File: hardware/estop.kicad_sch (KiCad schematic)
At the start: 2 parts

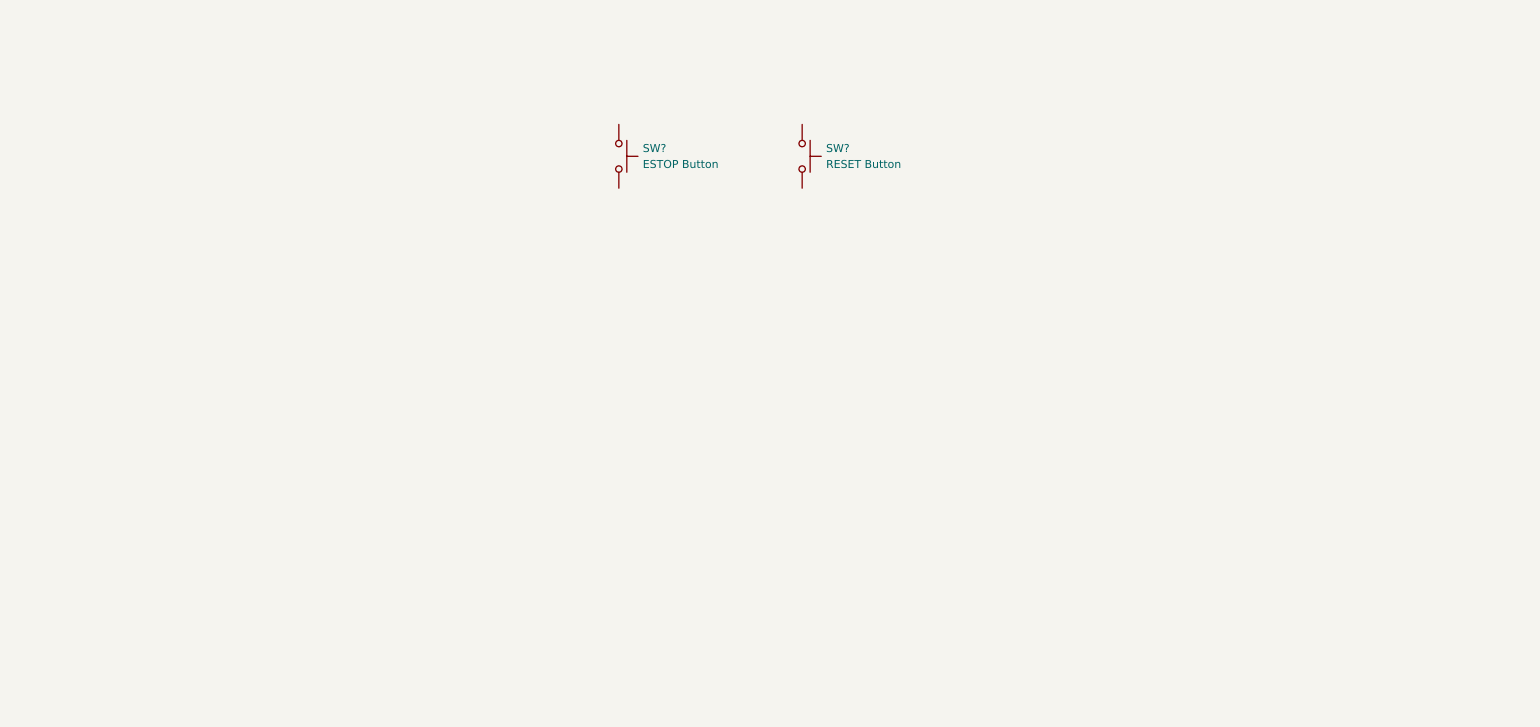
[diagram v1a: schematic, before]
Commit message: Begin ESTOP sheet
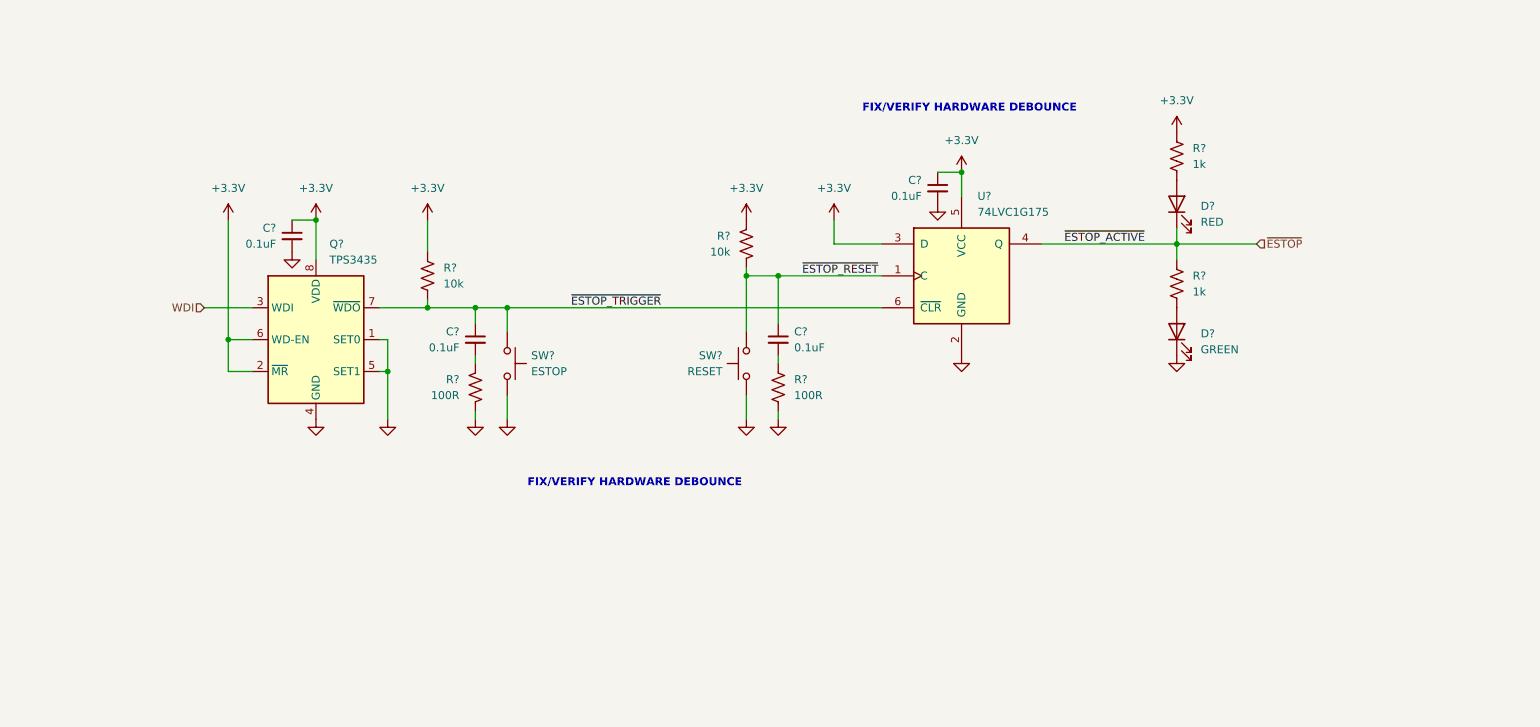
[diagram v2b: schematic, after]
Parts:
- added C? (x4): 0.1uF, Capacitor_SMD:C_0603_1608Metric_Pad1.08x0.95mm_HandSolder, symbol Device:C_Small
- added D?: GREEN, Diode_SMD:D_0805_2012Metric, symbol Device:LED
- added D?: RED, Diode_SMD:D_0805_2012Metric, symbol Device:LED
- added Q?: TPS3435, Package_TO_SOT_SMD:SOT-23-8, symbol stepping-stone:TPS3435CAGBJDDFRQ1
- added R? (x2): 10k, Resistor_SMD:R_0603_1608Metric, symbol Device:R_US
- added R? (x2): 1k, Resistor_SMD:R_0603_1608Metric, symbol Device:R_US
- added R? (x2): 100R, Resistor_SMD:R_0603_1608Metric, symbol Device:R_US
- added U?: 74LVC1G175, Package_TO_SOT_SMD:SOT-23-6, symbol 74xGxx:74LVC1G175
- SW?: value RESET Button -> RESET
- SW?: value ESTOP Button -> ESTOP
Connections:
- net ~{ESTOP_RESET}: now reaches SW?.1
- net ~{ESTOP_RESET}: now also C?.1, R?.2, U?.1 (C)
- net GND: now reaches SW?.2
- net GND: now also SW?.2, C?.2, C?.2, D?.1 (K), Q?.1 (SET0), Q?.4 (GND), Q?.5 (SET1), R?.1, R?.1, U?.2 (GND)
- net ~{ESTOP_TRIGGER}: now reaches SW?.1
- net ~{ESTOP_TRIGGER}: now also C?.1, Q?.7 (~{WDO}), R?.2, U?.6 (~{CLR})
- new net: D?.2 (A), R?.2 (x2)
- new net: C?.2, R?.2 (x2)
- new net +3.3V: C?.1, C?.1, Q?.2 (~{MR}), Q?.6 (WD-EN), Q?.8 (VDD), R?.1, R?.1, R?.1, U?.3 (D), U?.5 (VCC)
- new net WDI: Q?.3 (WDI)
- new net ~{ESTOP}: D?.1 (K), R?.1, U?.4 (Q)
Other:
- note added: "FIX/VERIFY HARDWARE DEBOUNCE"
- company: (none) -> Jacob Wigent
- title: (none) -> ESTOP System
- moved on the sheet: SW?

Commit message: Random changes & LED additions
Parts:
- U?: Part Number (none) -> SN74LVC1G175DBVR; Vendor URL (none) -> https://www.digikey.com/en/products/detail/texas-instrument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
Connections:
- net ~{ESTOP_TRIGGER} renamed ~{EXT_TRIG}
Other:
- note added: "ESTOP Button"
- note added: "ESTOP Triggers"
- note added: "External"
- note added: "External trigger should be driven by OPEN-DRAIN GPIO for safety."
- note added: "FIX/VERIFY HARDWARE DEBOUNCE FOR BOTH BUTTONS 74LVC MAY NEED SCHMITT TRIG INPUTS"
- note added: "Heartbeat Watchdog"
- note removed: "FIX/VERIFY HARDWARE DEBOUNCE"
- moved on the sheet: C?, D?, Q?, R?, SW?, U?

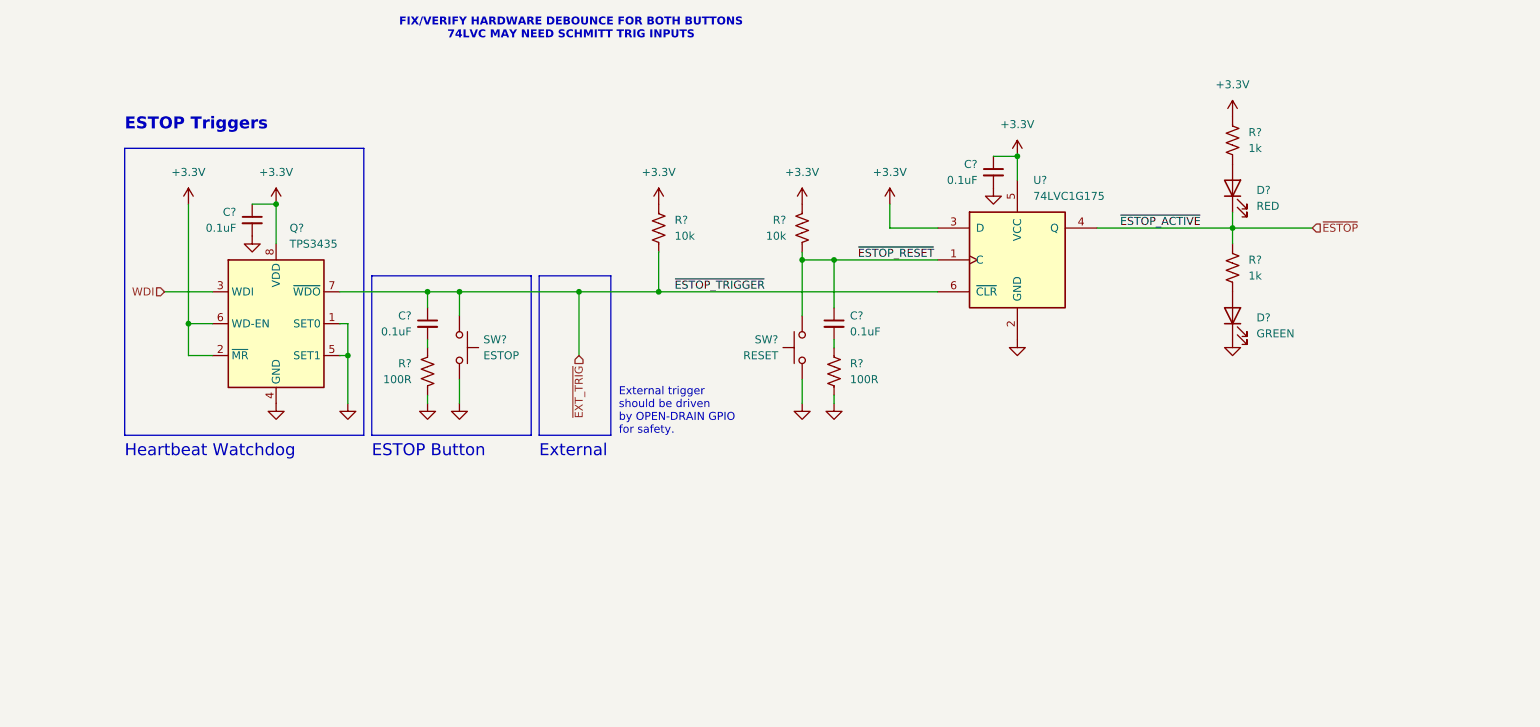
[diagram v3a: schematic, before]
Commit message: ESTOP control refinement
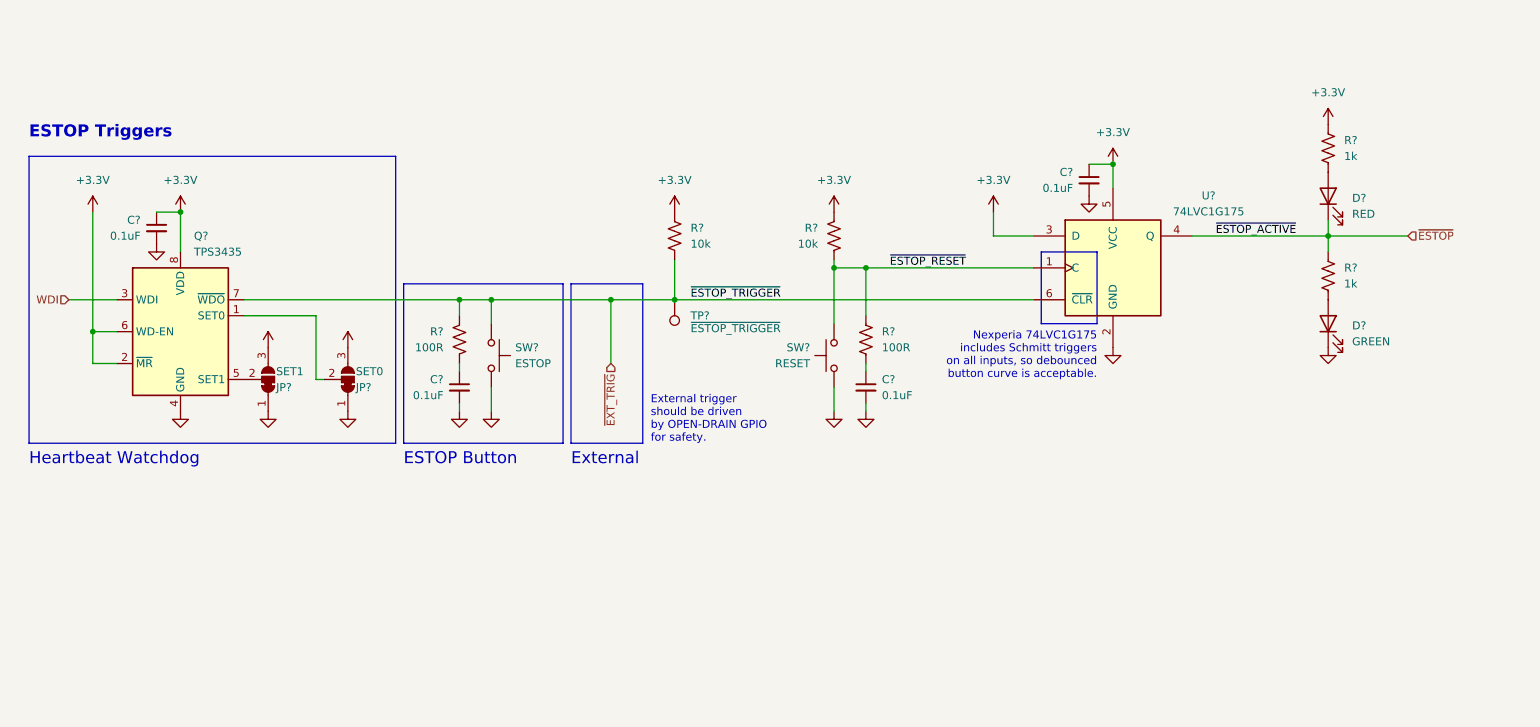
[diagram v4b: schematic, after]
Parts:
- removed C?: 0.1uF, Capacitor_SMD:C_0603_1608Metric_Pad1.08x0.95mm_HandSolder, symbol Device:C_Small
- removed R?: 100R, Resistor_SMD:R_0603_1608Metric, symbol Device:R_US
- removed U?: 74LVC1G175, Package_TO_SOT_SMD:SOT-23-6, symbol 74xGxx:74LVC1G175
- added C?: 0.1uF, Capacitor_SMD:C_0603_1608Metric_Pad1.08x0.95mm_HandSolder, symbol Device:C_Small
- added JP?: SET0, Jumper:SolderJumper-3_P1.3mm_Bridged12_RoundedPad1.0x1.5mm, symbol Jumper:SolderJumper_3_Bridged12
- added JP?: SET1, Jumper:SolderJumper-3_P1.3mm_Bridged12_RoundedPad1.0x1.5mm, symbol Jumper:SolderJumper_3_Bridged12
- added R?: 100R, Resistor_SMD:R_0603_1608Metric, symbol Device:R_US
- added TP?: ~{ESTOP_TRIGGER}, TestPoint:TestPoint_Pad_D1.0mm, symbol Connector:TestPoint
- added U?: 74LVC1G175, Package_TO_SOT_SMD:SOT-363_SC-70-6, symbol 74xGxx:74LVC1G175
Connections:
- net +3.3V: now also JP?.3 (B), JP?.3 (B), U?.3 (D), U?.5 (VCC)
- net GND: now also C?.2, C?.2, JP?.1 (A), JP?.1 (A), U?.2 (GND); no longer Q?.1 (SET0), Q?.5 (SET1), R?.1
- net ~{ESTOP_RESET}: now also R?.2, U?.1 (C)
- net ~{ESTOP}: now also U?.4 (Q)
- net ~{EXT_TRIG}: now also R?.2, TP?.1, U?.6 (~{CLR}); no longer C?.1
- new net: JP?.2 (C), Q?.1 (SET0)
- new net: JP?.2 (C), Q?.5 (SET1)
- new net: C?.1, R?.1 (x2)
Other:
- note added: "Nexperia 74LVC1G175 includes Schmitt triggers on all inputs, so debounced button curve is acceptable."
- note removed: "FIX/VERIFY HARDWARE DEBOUNCE FOR BOTH BUTTONS 74LVC MAY NEED SCHMITT TRIG INPUTS"
- moved on the sheet: C?, D?, Q?, R?, SW?

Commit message: SD Card Pull Ups and ESD
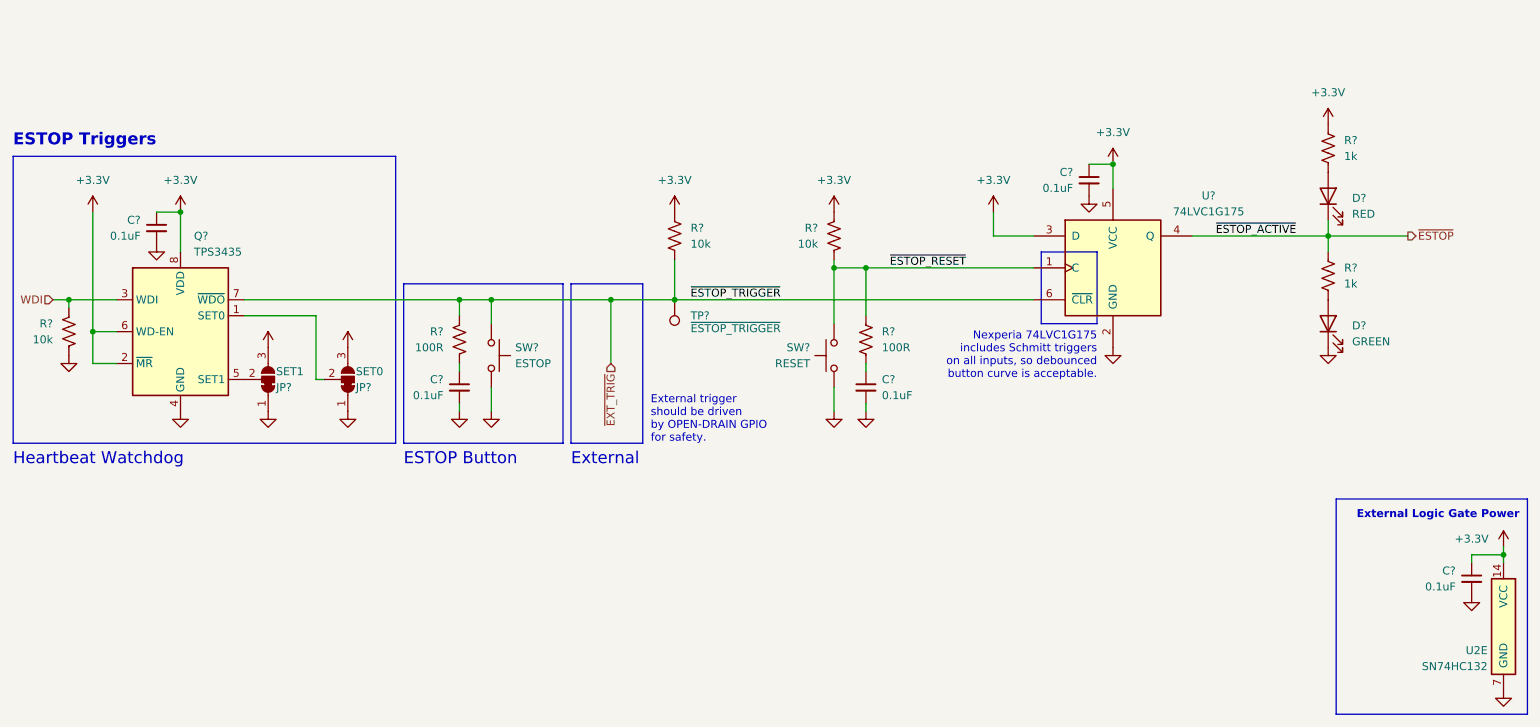
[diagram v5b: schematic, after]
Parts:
- added C?: 0.1uF, Capacitor_SMD:C_0603_1608Metric_Pad1.08x0.95mm_HandSolder, symbol Device:C_Small
- added R?: 10k, Resistor_SMD:R_0603_1608Metric, symbol Device:R_US
- added U2: SN74HC132, Package_SO:SOIC-14_3.9x8.7mm_P1.27mm, symbol stepping-stone:SN74LVC08
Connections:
- net +3.3V: now also C?.1, U2.14 (VCC)
- net GND: now also C?.2, R?.2, U2.7 (GND)
- net WDI: now also R?.1
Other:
- note added: "External Logic Gate Power"

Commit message: Add QSPI Flash
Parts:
- gave numbers to parts that had none: 21
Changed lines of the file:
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@@
 		(in_pos_files yes)
 		(dnp no)
-		(property "Reference" "R?"
+		(property "Reference" "R22"
 			(at 31.75 109.2199 0)
 			(show_name no)
@@
 			(project "stepping-stone"
 				(path "/793a882e-3f7b-468b-a863-41a1f527e1bf/ca68e3e0-6620-4c6d-b672-8e352c5602f5"
-					(reference "R?")
+					(reference "R22")
 					(unit 1)
 				)
@@
 		(in_pos_files yes)
 		(dnp no)
-		(property "Reference" "R?"
+		(property "Reference" "R19"
 			(at 133.35 93.9799 0)
 			(show_name no)
@@
 			(project "stepping-stone"
 				(path "/793a882e-3f7b-468b-a863-41a1f527e1bf/ca68e3e0-6620-4c6d-b672-8e352c5602f5"
-					(reference "R?")
+					(reference "R19")
 					(unit 1)
 				)
@@
 		(in_pos_files yes)
 		(dnp no)
-		(property "Reference" "C?"
+		(property "Reference" "C13"
 			(at 45.72 92.71 0)
 			(show_name no)
@@
 			(project "stepping-stone"
 				(path "/793a882e-3f7b-468b-a863-41a1f527e1bf/ca68e3e0-6620-4c6d-b672-8e352c5602f5"
-					(reference "C?")
+					(reference "C13")
 					(unit 1)
 				)
@@
 		(in_pos_files yes)
 		(dnp no)
-		(property "Reference" "R?"
+		(property "Reference" "R20"
 			(at 153.67 93.9799 0)
 			(show_name no)
@@
 			(project "stepping-stone"
 				(path "/793a882e-3f7b-468b-a863-41a1f527e1bf/ca68e3e0-6620-4c6d-b672-8e352c5602f5"
-					(reference "R?")
+					(reference "R20")
 					(unit 1)
 				)
@@
 		(dnp no)
 		(fields_autoplaced yes)
-		(property "Reference" "Q?"
+		(property "Reference" "Q3"
 			(at 54.2133 95.25 0)
 			(show_name no)
@@
 			(project "stepping-stone"
 				(path "/793a882e-3f7b-468b-a863-41a1f527e1bf/ca68e3e0-6620-4c6d-b672-8e352c5602f5"
-					(reference "Q?")
+					(reference "Q3")
 					(unit 1)
 				)
@@
 		(in_pos_files yes)
 		(dnp no)
-		(property "Reference" "SW?"
+		(property "Reference" "SW8"
 			(at 152.4 113.03 90)
 			(show_name no)
@@
 			(project "stepping-stone"
 				(path "/793a882e-3f7b-468b-a863-41a1f527e1bf/ca68e3e0-6620-4c6d-b672-8e352c5602f5"
-					(reference "SW?")
+					(reference "SW8")
 					(unit 1)
 				)
@@
 		(in_pos_files yes)
 		(dnp no)
-		(property "Reference" "C?"
+		(property "Reference" "C15"
 			(at 163.83 118.1162 0)
 			(show_name no)
@@
 			(project "stepping-stone"
 				(path "/793a882e-3f7b-468b-a863-41a1f527e1bf/ca68e3e0-6620-4c6d-b672-8e352c5602f5"
-					(reference "C?")
+					(reference "C15")
 					(unit 1)
 				)
@@
 		(in_pos_files yes)
 		(dnp no)
-		(property "Reference" "TP?"
+		(property "Reference" "TP1"
 			(at 133.35 107.95 0)
 			(show_name no)
@@
 			(project "stepping-stone"
 				(path "/793a882e-3f7b-468b-a863-41a1f527e1bf/ca68e3e0-6620-4c6d-b672-8e352c5602f5"
-					(reference "TP?")
+					(reference "TP1")
 					(unit 1)
 				)
@@
 		(dnp no)
 		(fields_autoplaced yes)
-		(property "Reference" "R?"
+		(property "Reference" "R21"
 			(at 237.49 100.3299 0)
 			(show_name no)
@@
 			(project "stepping-stone"
 				(path "/793a882e-3f7b-468b-a863-41a1f527e1bf/ca68e3e0-6620-4c6d-b672-8e352c5602f5"
-					(reference "R?")
+					(reference "R21")
 					(unit 1)
 				)
@@
 		(dnp no)
 		(fields_autoplaced yes)
-		(property "Reference" "D?"
+		(property "Reference" "D11"
 			(at 238.76 109.5374 90)
 			(show_name no)
@@
 			(project "stepping-stone"
 				(path "/793a882e-3f7b-468b-a863-41a1f527e1bf/ca68e3e0-6620-4c6d-b672-8e352c5602f5"
-					(reference "D?")
+					(reference "D11")
 					(unit 1)
 				)
@@
 		(in_pos_files yes)
 		(dnp no)
-		(property "Reference" "R?"
+		(property "Reference" "R24"
 			(at 163.83 110.49 0)
 			(show_name no)
@@
 			(project "stepping-stone"
 				(path "/793a882e-3f7b-468b-a863-41a1f527e1bf/ca68e3e0-6620-4c6d-b672-8e352c5602f5"
-					(reference "R?")
+					(reference "R24")
 					(unit 1)
 				)
@@
 		(in_pos_files yes)
 		(dnp no)
-		(property "Reference" "C?"
+		(property "Reference" "C14"
 			(at 93.98 118.1162 0)
 			(show_name no)
@@
 			(project "stepping-stone"
 				(path "/793a882e-3f7b-468b-a863-41a1f527e1bf/ca68e3e0-6620-4c6d-b672-8e352c5602f5"
-					(reference "C?")
+					(reference "C14")
 					(unit 1)
 				)
@@
 		(in_pos_files yes)
 		(dnp no)
-		(property "Reference" "R?"
+		(property "Reference" "R23"
 			(at 93.98 110.49 0)
 			(show_name no)
@@
 			(project "stepping-stone"
 				(path "/793a882e-3f7b-468b-a863-41a1f527e1bf/ca68e3e0-6620-4c6d-b672-8e352c5602f5"
-					(reference "R?")
+					(reference "R23")
 					(unit 1)
 				)
@@
 		(in_pos_files yes)
 		(dnp no)
-		(property "Reference" "SW?"
+		(property "Reference" "SW7"
 			(at 105.41 113.0299 90)
 			(show_name no)
@@
 			(project "stepping-stone"
 				(path "/793a882e-3f7b-468b-a863-41a1f527e1bf/ca68e3e0-6620-4c6d-b672-8e352c5602f5"
-					(reference "SW?")
+					(reference "SW7")
 					(unit 1)
 				)
@@
 		(in_pos_files yes)
 		(dnp no)
-		(property "Reference" "JP?"
+		(property "Reference" "JP2"
 			(at 80.01 119.38 90)
 			(show_name no)
@@
 			(project "stepping-stone"
 				(path "/793a882e-3f7b-468b-a863-41a1f527e1bf/ca68e3e0-6620-4c6d-b672-8e352c5602f5"
-					(reference "JP?")
+					(reference "JP2")
 					(unit 1)
 				)
@@
 		(in_pos_files yes)
 		(dnp no)
-		(property "Reference" "C?"
+		(property "Reference" "C16"
 			(at 255.27 148.5962 0)
 			(show_name no)
@@
 			(project "stepping-stone"
 				(path "/793a882e-3f7b-468b-a863-41a1f527e1bf/ca68e3e0-6620-4c6d-b672-8e352c5602f5"
-					(reference "C?")
+					(reference "C16")
 					(unit 1)
 				)
@@
 		(in_pos_files yes)
 		(dnp no)
-		(property "Reference" "JP?"
+		(property "Reference" "JP1"
 			(at 67.31 119.38 90)
 			(show_name no)
@@
 			(project "stepping-stone"
 				(path "/793a882e-3f7b-468b-a863-41a1f527e1bf/ca68e3e0-6620-4c6d-b672-8e352c5602f5"
-					(reference "JP?")
+					(reference "JP1")
 					(unit 1)
 				)
@@
 		(dnp no)
 		(fields_autoplaced yes)
-		(property "Reference" "D?"
+		(property "Reference" "D10"
 			(at 238.76 89.2174 90)
 			(show_name no)
@@
 			(project "stepping-stone"
 				(path "/793a882e-3f7b-468b-a863-41a1f527e1bf/ca68e3e0-6620-4c6d-b672-8e352c5602f5"
-					(reference "D?")
+					(reference "D10")
 					(unit 1)
 				)
@@
 		(in_pos_files yes)
 		(dnp no)
-		(property "Reference" "C?"
+		(property "Reference" "C12"
 			(at 194.31 85.09 0)
 			(show_name no)
@@
 			(project "stepping-stone"
 				(path "/793a882e-3f7b-468b-a863-41a1f527e1bf/ca68e3e0-6620-4c6d-b672-8e352c5602f5"
-					(reference "C?")
+					(reference "C12")
 					(unit 1)
 				)
@@
 		(dnp no)
 		(fields_autoplaced yes)
-		(property "Reference" "R?"
+		(property "Reference" "R18"
 			(at 237.49 80.0099 0)
 			(show_name no)
@@
 			(project "stepping-stone"
 				(path "/793a882e-3f7b-468b-a863-41a1f527e1bf/ca68e3e0-6620-4c6d-b672-8e352c5602f5"
-					(reference "R?")
+					(reference "R18")
 					(unit 1)
 				)
@@
 		(dnp no)
 		(fields_autoplaced yes)
-		(property "Reference" "U?"
+		(property "Reference" "U4"
 			(at 215.9 88.8298 0)
 			(show_name no)
@@
 			(project "stepping-stone"
 				(path "/793a882e-3f7b-468b-a863-41a1f527e1bf/ca68e3e0-6620-4c6d-b672-8e352c5602f5"
-					(reference "U?")
+					(reference "U4")
 					(unit 1)
 				)

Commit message: Fix Designators (Q -> U)
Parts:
- renumbered Q3 to U?
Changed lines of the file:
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@@
 		(dnp no)
 		(fields_autoplaced yes)
-		(property "Reference" "Q3"
+		(property "Reference" "U?"
 			(at 54.2133 95.25 0)
 			(show_name no)
@@
 			(project "stepping-stone"
 				(path "/793a882e-3f7b-468b-a863-41a1f527e1bf/ca68e3e0-6620-4c6d-b672-8e352c5602f5"
-					(reference "Q3")
+					(reference "U?")
 					(unit 1)
 				)
